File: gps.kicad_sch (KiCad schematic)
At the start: 14 parts, among them IC2 TESEO-LIV3F, IC3 BGA_725L6_E6327

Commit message: Add company name (using github URL), date, and change revision number to all schematic pages
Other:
- company: (none) -> github.com/fuad1502/open-running-watch-hw
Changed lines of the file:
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@@
 	(title_block
 		(title "Open Running Watch")
-		(rev "A")
+		(date "2024-04-12")
+		(rev "0.1.0")
+		(company "github.com/fuad1502/open-running-watch-hw")
 	)

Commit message: Changed hand soldered footprints to normal footprints
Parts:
- C15, C16, C17, C18, C19, C20, C21: footprint Capacitor_SMD:C_0402_1005Metric_Pad0.74x0.62mm_HandSolder -> Capacitor_SMD:C_0402_1005Metric
- L2, L3: footprint Inductor_SMD:L_0402_1005Metric_Pad0.77x0.64mm_HandSolder -> Inductor_SMD:L_0402_1005Metric
- R5: footprint Resistor_SMD:R_0402_1005Metric_Pad0.72x0.64mm_HandSolder -> Resistor_SMD:R_0402_1005Metric

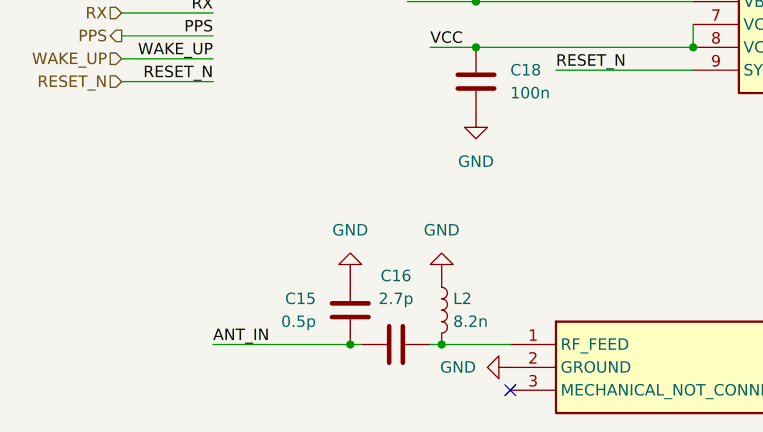
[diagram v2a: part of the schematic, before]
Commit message: Changed GNSS antenna matching to world wide setting
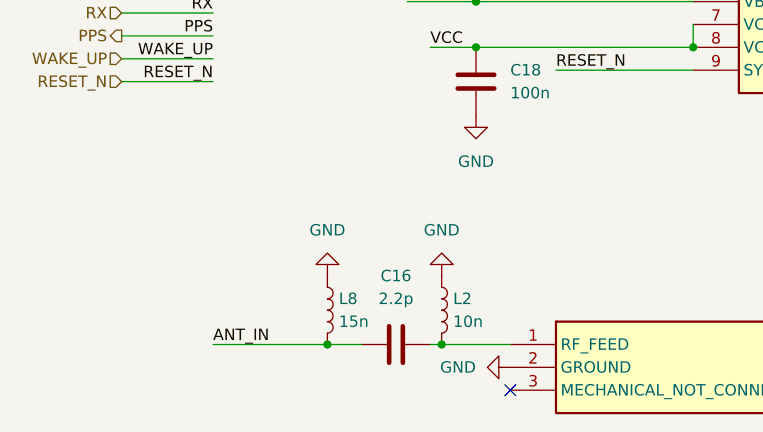
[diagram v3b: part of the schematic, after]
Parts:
- removed C15: 0.5p, Capacitor_SMD:C_0402_1005Metric, symbol Device:C
- added L8: 15n, Inductor_SMD:L_0402_1005Metric, symbol Device:L
- C16: value 2.7p -> 2.2p; Manufacturer_Part_Number GCM1555C1H2R7BA16D -> GRM1555C1H2R2CA01D
- L2: value 8.2n -> 10n; Manufacturer_Part_Number LQG15HS8N2G02D -> LQG15HS10NH02D
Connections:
- net ANT_IN: now also L8.2
- net GND: now also L8.1
